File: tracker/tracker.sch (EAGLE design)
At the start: 19 parts, among them U1 ATXMEGA128A3-AU, U2 VENUS638FLPX-L

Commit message: xmega now connected to pdi connector
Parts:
- added J1: (no value), SparkFun-Connectors:JST_2MM_MALE
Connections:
- new net PDI_CLK: R1.1, U$2.CLK, U1.!RESET!/PDI
- new net PDI_DATA: U$2.DATA, U1.PDI
- net 3.3V: now also R1.2, U$2.VCC, U1.AVCC, U1.VCC
- net GND: now also U$2.GND
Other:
- moved on the sheet: C1, C2, C3, C4, C5, C6, R1, U$1, U$2, U1

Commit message: initial steps for the charging/power circuit
 * micro usb port added
 * 2-pin jst battery connector added
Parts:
- added U$4: USB, rocket:USB
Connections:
- new net VIN: U$4.VBUS
- net GND: now also U$4.GND
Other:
- moved on the sheet: C1, C2, C3, C4, C5, C6, C7, C8, J1, L1, R1, R2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

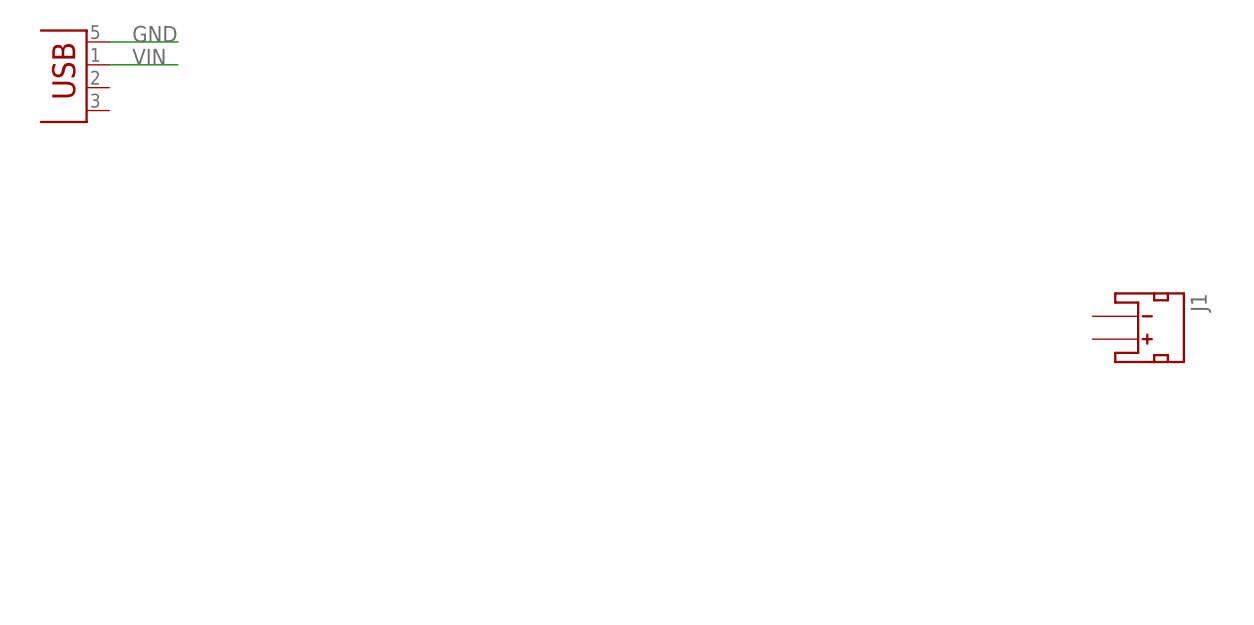
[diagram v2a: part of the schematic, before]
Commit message: Initial power connection
* Added charging IC
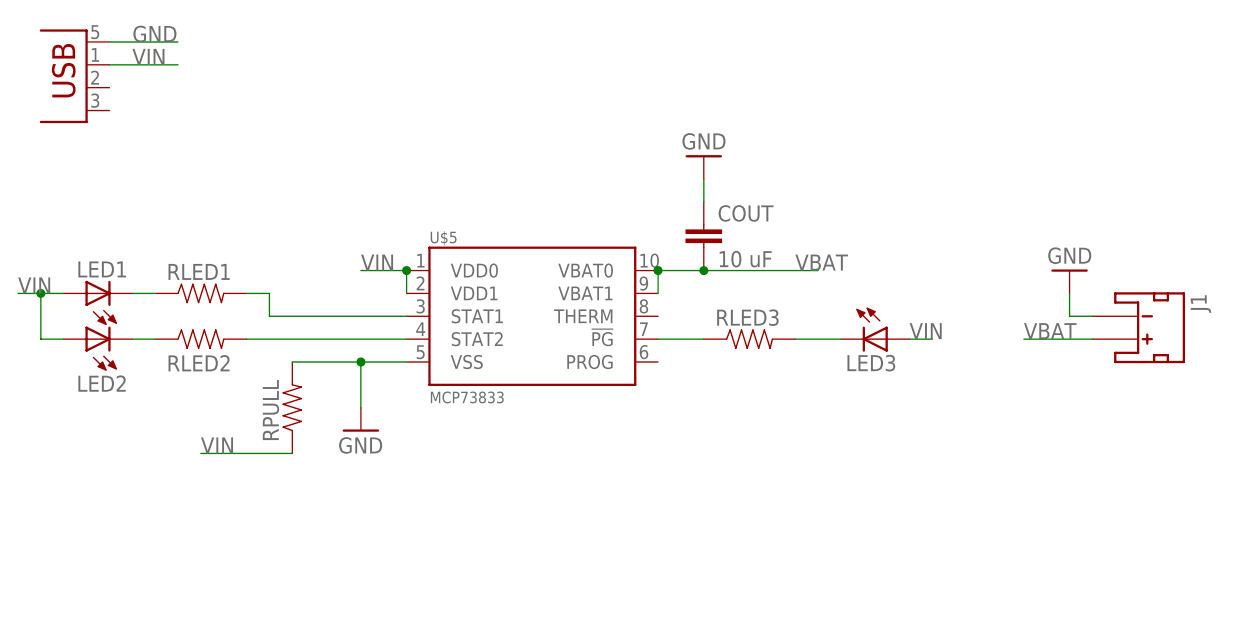
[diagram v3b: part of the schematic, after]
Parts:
- added COUT: 10 uF, SparkFun:CAP0805
- added LED1, LED2, LED3: (no value), led:LEDCHIP-LED0805
- added RLED1, RLED2, RLED3, RPULL: (no value), SparkFun:RESISTOR0805-RES
- added U$5: MCP73833, rocket:MCP73833
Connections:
- new net N$3: RLED3.1, U$5.!PG
- new net N$4: RLED2.2, U$5.STAT2
- new net N$5: RLED1.2, U$5.STAT1
- new net N$6: LED1.C, RLED1.1
- new net N$7: LED2.C, RLED2.1
- new net N$8: LED3.C, RLED3.2
- net GND: now also COUT.1, J1.-, RPULL.2, U$5.VSS
- net VBAT: now also COUT.2, J1.+, U$5.VBAT0, U$5.VBAT1
- net VIN: now also LED1.A, LED2.A, LED3.A, RPULL.1, U$5.VDD0, U$5.VDD1
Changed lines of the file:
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@@
 <part name="FRAME1" library="frames" deviceset="FRAME_B_L" device=""/>
 <part name="U$4" library="rocket" deviceset="USB" device=""/>
+<part name="U$5" library="rocket" deviceset="MCP73833" device=""/>
+<part name="RLED1" library="SparkFun" deviceset="RESISTOR" device="0805-RES"/>
+<part name="RLED2" library="SparkFun" deviceset="RESISTOR" device="0805-RES"/>
+<part name="RLED3" library="SparkFun" deviceset="RESISTOR" device="0805-RES"/>
+<part name="RPULL" library="SparkFun" deviceset="RESISTOR" device="0805-RES"/>
+<part name="GND13" library="SparkFun" deviceset="GND" device=""/>
+<part name="GND14" library="SparkFun" deviceset="GND" device=""/>
+<part name="LED1" library="led" deviceset="LED" device="CHIP-LED0805"/>
+<part name="LED2" library="led" deviceset="LED" device="CHIP-LED0805"/>
+<part name="LED3" library="led" deviceset="LED" device="CHIP-LED0805"/>
+<part name="COUT" library="SparkFun" deviceset="CAP" device="0805" value="10 uF"/>
+<part name="GND15" library="SparkFun" deviceset="GND" device=""/>
 </parts>
 <sheets>
@@
 <instance part="FRAME1" gate="G$2" x="325.12" y="0"/>
 <instance part="U$4" gate="G$1" x="15.24" y="266.7" rot="R180"/>
+<instance part="U$5" gate="G$1" x="58.42" y="228.6"/>
+<instance part="RLED1" gate="G$1" x="33.02" y="238.76"/>
+<instance part="RLED2" gate="G$1" x="33.02" y="233.68" smashed="yes">
+<attribute name="NAME" x="29.21" y="230.0986" size="1.778" layer="95"/>
+<attribute name="VALUE" x="29.21" y="230.378" size="1.778" layer="96"/>
+</instance>
+<instance part="RLED3" gate="G$1" x="93.98" y="233.68"/>
+<instance part="RPULL" gate="G$1" x="43.18" y="226.06" rot="R90"/>
+<instance part="GND13" gate="1" x="129.54" y="241.3" rot="R180"/>
+<instance part="GND14" gate="1" x="50.8" y="223.52"/>
+<instance part="LED1" gate="G$1" x="20.32" y="238.76" smashed="yes" rot="R90">
+<attribute name="NAME" x="24.892" y="242.316" size="1.778" layer="95" rot="R180"/>
+<attribute name="VALUE" x="24.892" y="244.475" size="1.778" layer="96" rot="R180"/>
+</instance>
+<instance part="LED2" gate="G$1" x="20.32" y="233.68" smashed="yes" rot="R90">
+<attribute name="NAME" x="24.892" y="229.616" size="1.778" layer="95" rot="R180"/>
+<attribute name="VALUE" x="24.892" y="239.395" size="1.778" layer="96" rot="R180"/>
+</instance>
+<instance part="LED3" gate="G$1" x="109.22" y="233.68" rot="R270"/>
+<instance part="COUT" gate="G$1" x="88.9" y="243.84"/>
+<instance part="GND15" gate="1" x="88.9" y="254" rot="R180"/>
 </instances>
 <busses>
@@
 <wire x1="22.86" y1="266.7" x2="30.48" y2="266.7" width="0.1524" layer="91"/>
 <label x="25.4" y="266.7" size="1.778" layer="95"/>
+</segment>
+<segment>
+<pinref part="U$5" gate="G$1" pin="VSS"/>
+<pinref part="GND14" gate="1" pin="GND"/>
+<wire x1="55.88" y1="231.14" x2="50.8" y2="231.14" width="0.1524" layer="91"/>
+<wire x1="50.8" y1="231.14" x2="50.8" y2="226.06" width="0.1524" layer="91"/>
+<pinref part="RPULL" gate="G$1" pin="2"/>
+<wire x1="43.18" y1="231.14" x2="50.8" y2="231.14" width="0.1524" layer="91"/>
+<junction x="50.8" y="231.14"/>
+</segment>
+<segment>
+<pinref part="GND13" gate="1" pin="GND"/>
+<wire x1="129.54" y1="238.76" x2="129.54" y2="236.22" width="0.1524" layer="91"/>
+<pinref part="J1" gate="G$1" pin="-"/>
+<wire x1="129.54" y1="236.22" x2="132.08" y2="236.22" width="0.1524" layer="91"/>
+</segment>
+<segment>
+<pinref part="GND15" gate="1" pin="GND"/>
+<pinref part="COUT" gate="G$1" pin="1"/>
+<wire x1="88.9" y1="251.46" x2="88.9" y2="248.92" width="0.1524" layer="91"/>
 </segment>
 </net>
@@
 <label x="342.9" y="129.54" size="1.778" layer="95"/>
 </segment>
+<segment>
+<pinref part="COUT" gate="G$1" pin="2"/>
+<pinref part="U$5" gate="G$1" pin="VBAT0"/>
+<wire x1="88.9" y1="241.3" x2="83.82" y2="241.3" width="0.1524" layer="91"/>
+<pinref part="U$5" gate="G$1" pin="VBAT1"/>
+<wire x1="83.82" y1="238.76" x2="83.82" y2="241.3" width="0.1524" layer="91"/>
+<junction x="83.82" y="241.3"/>
+<wire x1="88.9" y1="241.3" x2="101.6" y2="241.3" width="0.1524" layer="91"/>
+<junction x="88.9" y="241.3"/>
+<label x="99.06" y="241.3" size="1.778" layer="95"/>
+</segment>
+<segment>
+<pinref part="J1" gate="G$1" pin="+"/>
+<wire x1="132.08" y1="233.68" x2="124.46" y2="233.68" width="0.1524" layer="91"/>
+<label x="124.46" y="233.68" size="1.778" layer="95"/>
+</segment>
 </net>
 <net name="RSTN" class="0">
@@
 <label x="25.4" y="264.16" size="1.778" layer="95"/>
 </segment>
-</net>
+<segment>
+<pinref part="U$5" gate="G$1" pin="VDD0"/>
+<wire x1="50.8" y1="241.3" x2="55.88" y2="241.3" width="0.1524" layer="91"/>
+<label x="50.8" y="241.3" size="1.778" layer="95"/>
+<pinref part="U$5" gate="G$1" pin="VDD1"/>
+<wire x1="55.88" y1="238.76" x2="55.88" y2="241.3" width="0.1524" layer="91"/>
+<junction x="55.88" y="241.3"/>
+</segment>
+<segment>
+<pinref part="LED2" gate="G$1" pin="A"/>
+<wire x1="17.78" y1="233.68" x2="15.24" y2="233.68" width="0.1524" layer="91"/>
+<wire x1="15.24" y1="233.68" x2="15.24" y2="238.76" width="0.1524" layer="91"/>
+<wire x1="15.24" y1="238.76" x2="12.7" y2="238.76" width="0.1524" layer="91"/>
+<pinref part="LED1" gate="G$1" pin="A"/>
+<wire x1="17.78" y1="238.76" x2="15.24" y2="238.76" width="0.1524" layer="91"/>
+<junction x="15.24" y="238.76"/>
+<label x="12.7" y="238.76" size="1.778" layer="95"/>
+</segment>
+<segment>
+<pinref part="LED3" gate="G$1" pin="A"/>
+<wire x1="111.76" y1="233.68" x2="114.3" y2="233.68" width="0.1524" layer="91"/>
+<label x="111.76" y="233.68" size="1.778" layer="95"/>
+</segment>
+<segment>
+<pinref part="RPULL" gate="G$1" pin="1"/>
+<wire x1="43.18" y1="220.98" x2="33.02" y2="220.98" width="0.1524" layer="91"/>
+<label x="33.02" y="220.98" size="1.778" layer="95"/>
+</segment>
+</net>
+<net name="N$4" class="0">
+<segment>
+<pinref part="RLED2" gate="G$1" pin="2"/>
+<pinref part="U$5" gate="G$1" pin="STAT2"/>
+<wire x1="38.1" y1="233.68" x2="55.88" y2="233.68" width="0.1524" layer="91"/>
+</segment>
+</net>
+<net name="N$5" class="0">
+<segment>
+<pinref part="U$5" gate="G$1" pin="STAT1"/>
+<wire x1="55.88" y1="236.22" x2="40.64" y2="236.22" width="0.1524" layer="91"/>
+<wire x1="40.64" y1="236.22" x2="40.64" y2="238.76" width="0.1524" layer="91"/>
+<pinref part="RLED1" gate="G$1" pin="2"/>
+<wire x1="40.64" y1="238.76" x2="38.1" y2="238.76" width="0.1524" layer="91"/>
+</segment>
+</net>
+<net name="N$3" class="0">
+<segment>
+<pinref part="U$5" gate="G$1" pin="!PG"/>
+<pinref part="RLED3" gate="G$1" pin="1"/>
+<wire x1="83.82" y1="233.68" x2="88.9" y2="233.68" width="0.1524" layer="91"/>
+</segment>
+</net>
+<net name="N$6" class="0">
+<segment>
+<pinref part="LED1" gate="G$1" pin="C"/>
+<pinref part="RLED1" gate="G$1" pin="1"/>
+<wire x1="25.4" y1="238.76" x2="27.94" y2="238.76" width="0.1524" layer="91"/>
+</segment>
+</net>
+<net name="N$7" class="0">
+<segment>
+<pinref part="LED2" gate="G$1" pin="C"/>
+<pinref part="RLED2" gate="G$1" pin="1"/>
+<wire x1="25.4" y1="233.68" x2="27.94" y2="233.68" width="0.1524" layer="91"/>
+</segment>
+</net>
+<net name="N$8" class="0">
+<segment>
+<pinref part="RLED3" gate="G$1" pin="2"/>
+<pinref part="LED3" gate="G$1" pin="C"/>
+<wire x1="99.06" y1="233.68" x2="104.14" y2="233.68" width="0.1524" layer="91"/>
+</segment>
+</net>

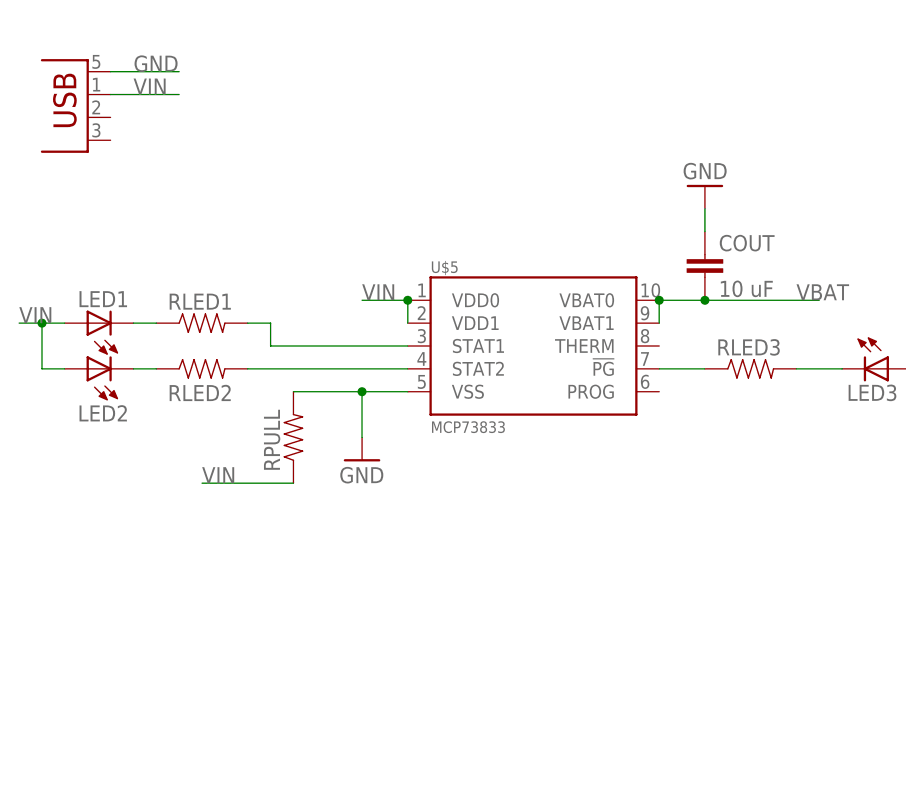
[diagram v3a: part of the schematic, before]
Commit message: Updates to charging circuit
* completed all connections for the charging circuit, except the
thermistor as it is still undecided how we will deal with that.
* still need to choose a voltage regulator and add it between the
battery and main circuit.
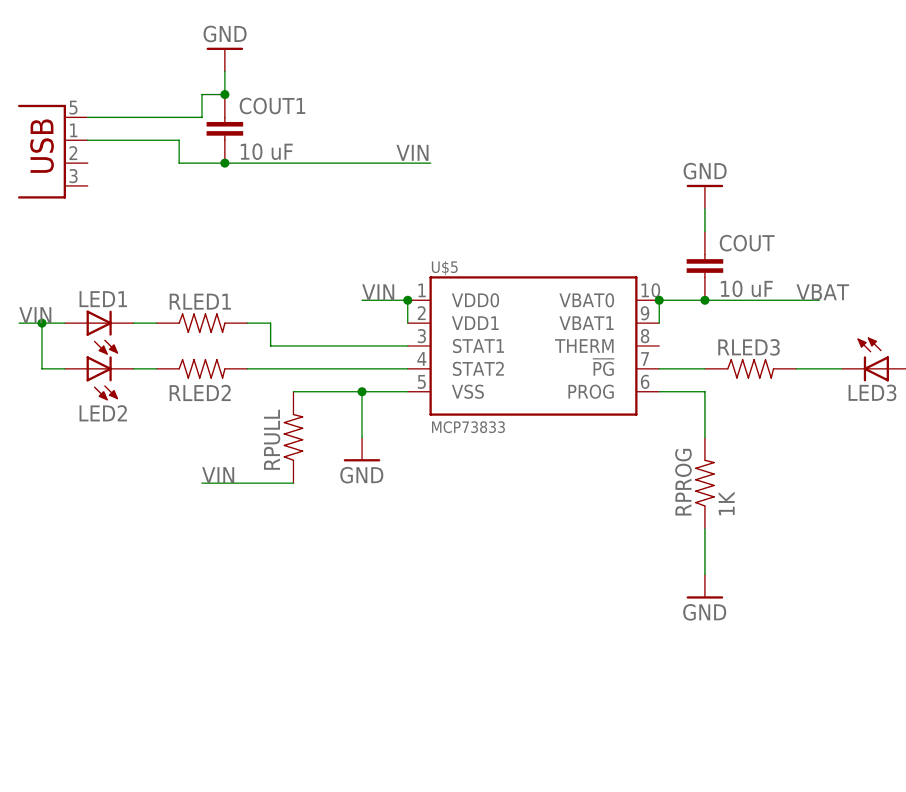
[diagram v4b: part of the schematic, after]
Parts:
- added COUT1: 10 uF, SparkFun:CAP0805
- added RPROG: 1K, SparkFun:RESISTOR0805-RES
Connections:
- new net N$12: RPROG.2, U$5.PROG
- net GND: now also COUT1.1, RPROG.1
- net VIN: now also COUT1.2
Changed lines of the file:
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@@
 <part name="COUT" library="SparkFun" deviceset="CAP" device="0805" value="10 uF"/>
 <part name="GND15" library="SparkFun" deviceset="GND" device=""/>
+<part name="COUT1" library="SparkFun" deviceset="CAP" device="0805" value="10 uF"/>
+<part name="GND16" library="SparkFun" deviceset="GND" device=""/>
+<part name="RPROG" library="SparkFun" deviceset="RESISTOR" device="0805-RES" value="1K"/>
+<part name="GND17" library="SparkFun" deviceset="GND" device=""/>
 </parts>
 <sheets>
@@
 <instance part="FRAME1" gate="G$1" x="0" y="0"/>
 <instance part="FRAME1" gate="G$2" x="325.12" y="0"/>
-<instance part="U$4" gate="G$1" x="15.24" y="266.7" rot="R180"/>
+<instance part="U$4" gate="G$1" x="12.7" y="261.62" rot="R180"/>
 <instance part="U$5" gate="G$1" x="58.42" y="228.6"/>
 <instance part="RLED1" gate="G$1" x="33.02" y="238.76"/>
@@
 <instance part="COUT" gate="G$1" x="88.9" y="243.84"/>
 <instance part="GND15" gate="1" x="88.9" y="254" rot="R180"/>
+<instance part="COUT1" gate="G$1" x="35.56" y="259.08"/>
+<instance part="GND16" gate="1" x="35.56" y="269.24" rot="R180"/>
+<instance part="RPROG" gate="G$1" x="88.9" y="220.98" rot="R90"/>
+<instance part="GND17" gate="1" x="88.9" y="208.28"/>
 </instances>
 <busses>
@@
 <segment>
 <pinref part="U$4" gate="G$1" pin="GND"/>
-<wire x1="22.86" y1="266.7" x2="30.48" y2="266.7" width="0.1524" layer="91"/>
-<label x="25.4" y="266.7" size="1.778" layer="95"/>
+<wire x1="20.32" y1="261.62" x2="33.02" y2="261.62" width="0.1524" layer="91"/>
+<pinref part="COUT1" gate="G$1" pin="1"/>
+<wire x1="35.56" y1="264.16" x2="33.02" y2="264.16" width="0.1524" layer="91"/>
+<wire x1="33.02" y1="264.16" x2="33.02" y2="261.62" width="0.1524" layer="91"/>
+<wire x1="35.56" y1="264.16" x2="35.56" y2="266.7" width="0.1524" layer="91"/>
+<junction x="35.56" y="264.16"/>
+<pinref part="GND16" gate="1" pin="GND"/>
 </segment>
 <segment>
@@
 <pinref part="COUT" gate="G$1" pin="1"/>
 <wire x1="88.9" y1="251.46" x2="88.9" y2="248.92" width="0.1524" layer="91"/>
+</segment>
+<segment>
+<pinref part="GND17" gate="1" pin="GND"/>
+<pinref part="RPROG" gate="G$1" pin="1"/>
+<wire x1="88.9" y1="210.82" x2="88.9" y2="215.9" width="0.1524" layer="91"/>
 </segment>
 </net>
@@
 <segment>
 <pinref part="U$4" gate="G$1" pin="VBUS"/>
-<wire x1="22.86" y1="264.16" x2="30.48" y2="264.16" width="0.1524" layer="91"/>
-<label x="25.4" y="264.16" size="1.778" layer="95"/>
+<wire x1="20.32" y1="259.08" x2="30.48" y2="259.08" width="0.1524" layer="91"/>
+<label x="54.61" y="256.794" size="1.778" layer="95"/>
+<wire x1="30.48" y1="259.08" x2="30.48" y2="256.54" width="0.1524" layer="91"/>
+<pinref part="COUT1" gate="G$1" pin="2"/>
+<wire x1="30.48" y1="256.54" x2="35.56" y2="256.54" width="0.1524" layer="91"/>
+<wire x1="35.56" y1="256.54" x2="58.42" y2="256.54" width="0.1524" layer="91"/>
+<junction x="35.56" y="256.54"/>
 </segment>
 <segment>
@@
 </segment>
 </net>
+<net name="N$12" class="0">
+<segment>
+<pinref part="U$5" gate="G$1" pin="PROG"/>
+<pinref part="RPROG" gate="G$1" pin="2"/>
+<wire x1="83.82" y1="231.14" x2="88.9" y2="231.14" width="0.1524" layer="91"/>
+<wire x1="88.9" y1="231.14" x2="88.9" y2="226.06" width="0.1524" layer="91"/>
+</segment>
+</net>
